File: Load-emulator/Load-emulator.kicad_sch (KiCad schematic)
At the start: 16 parts, among them J1 533980771, J2 SSW-126-04-G-D, J3 SSW-126-04-G-D, Q1 TIP41C, U1 LM324A

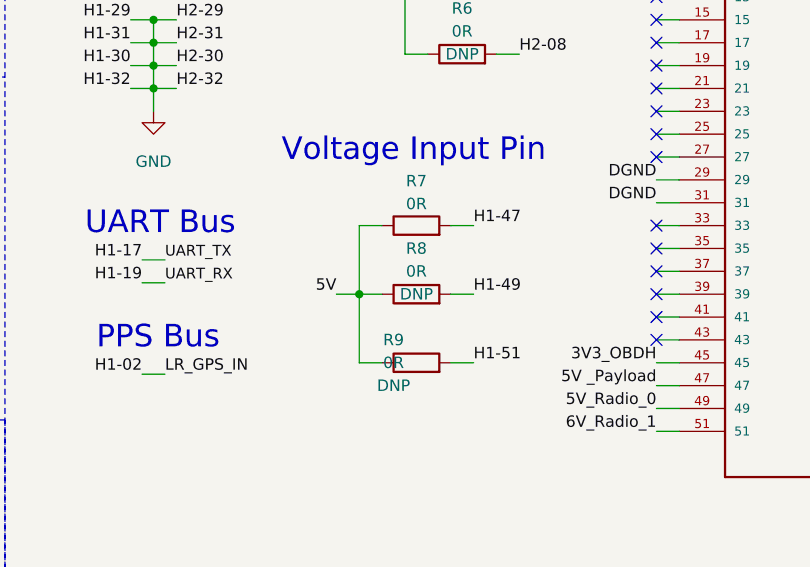
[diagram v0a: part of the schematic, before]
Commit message: Minor changes in schematic, add LM324N
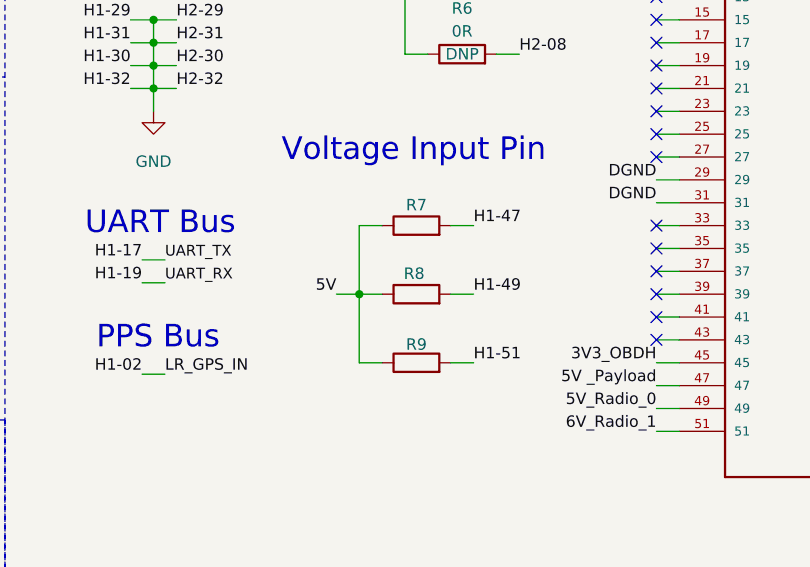
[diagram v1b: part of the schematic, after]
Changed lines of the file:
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@@
 		(dnp no)
 		(property "Reference" "R7"
-			(at 153.67 61.087 90)
+			(at 153.67 63.754 90)
 			(effects
 				(font
@@
 					(size 1.27 1.27)
 				)
+				(hide yes)
 			)
 		)
@@
 		(dnp no)
 		(property "Reference" "R9"
-			(at 151.13 78.74 90)
+			(at 153.67 79.248 90)
 			(effects
 				(font
@@
 		)
 		(property "Value" "0R"
-			(at 151.13 81.28 90)
-			(effects
-				(font
-					(size 1.27 1.27)
-				)
+			(at 155.194 83.82 90)
+			(effects
+				(font
+					(size 1.27 1.27)
+				)
+				(hide yes)
 			)
 		)
@@
 					(size 1.27 1.27)
 				)
+				(hide yes)
 			)
 		)
@@
 		(dnp no)
 		(property "Reference" "R8"
-			(at 153.67 68.58 90)
+			(at 153.416 71.374 90)
 			(effects
 				(font
@@
 					(size 1.27 1.27)
 				)
+				(hide yes)
 			)
 		)
@@
 					(size 1.27 1.27)
 				)
-			)
-		)
+				(hide yes)
+			)
+		)

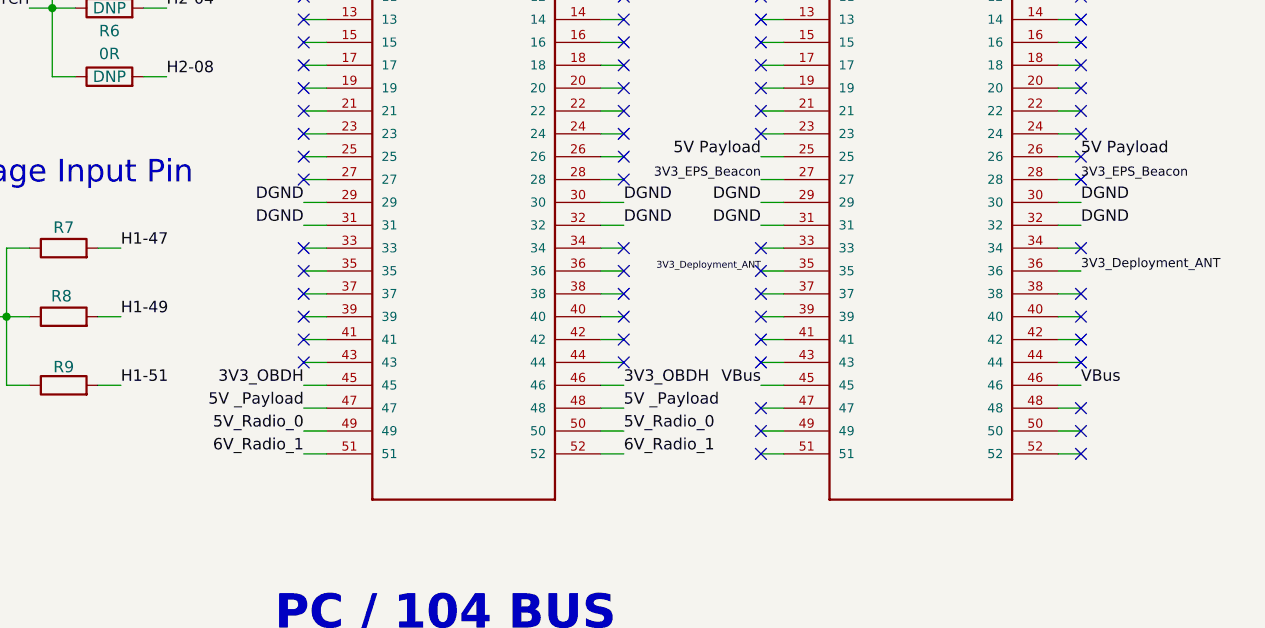
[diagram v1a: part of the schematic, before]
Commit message: Added new connector: PicoLock, as an alternative to the PC104. Connections between the two were made, so either one can be used.
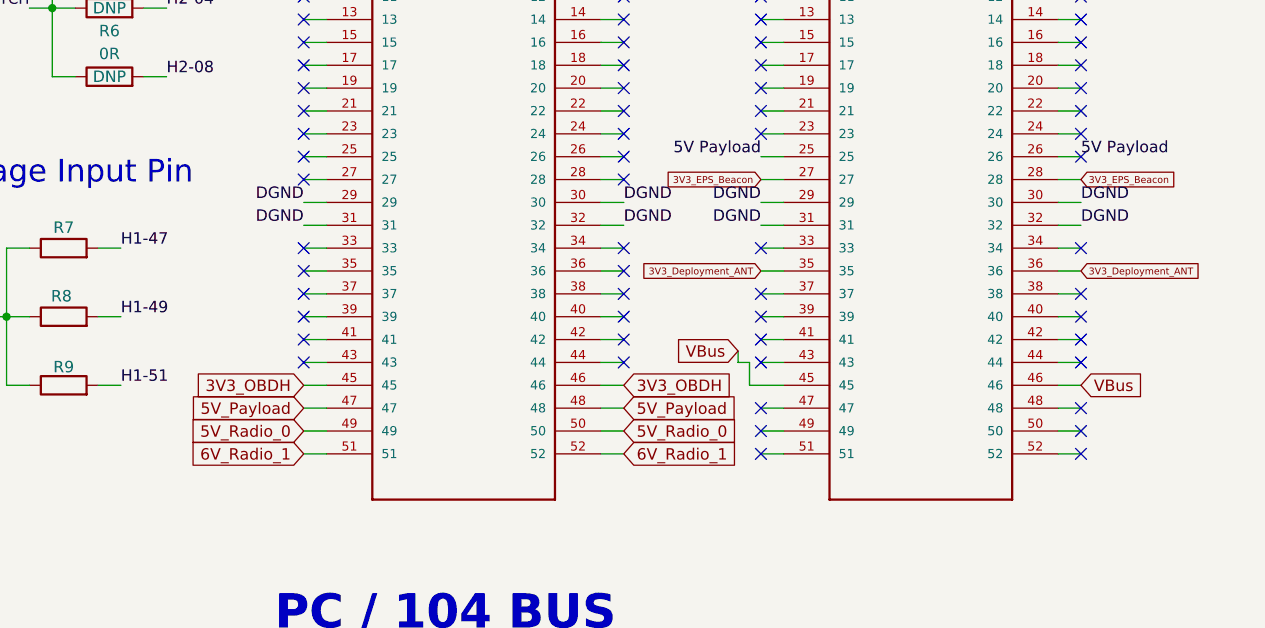
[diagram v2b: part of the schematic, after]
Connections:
- net 5V _Payload renamed 5V_Payload
- no-connect marks 83 -> 81

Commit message: Added footprints for the remaining resistors, capacitors and ampops, as well as some 3D models
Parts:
- Q1: footprint Package_TO_SOT_THT:TO-220-3_Vertical -> (none)
- R4, R5, R6, R7, R8, R9: footprint Resistor_SMD:R_0603_1608Metric_Pad0.98x0.95mm_HandSolder -> (none)
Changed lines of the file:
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@@
 			)
 		)
-		(property "Footprint" "Resistor_SMD:R_0603_1608Metric_Pad0.98x0.95mm_HandSolder"
+		(property "Footprint" ""
 			(at 158.75 41.148 90)
 			(effects
@@
 			)
 		)
-		(property "Footprint" "Resistor_SMD:R_0603_1608Metric_Pad0.98x0.95mm_HandSolder"
+		(property "Footprint" ""
 			(at 153.67 67.818 90)
 			(effects
@@
 			)
 		)
-		(property "Footprint" "Resistor_SMD:R_0603_1608Metric_Pad0.98x0.95mm_HandSolder"
+		(property "Footprint" ""
 			(at 153.67 83.058 90)
 			(effects
@@
 			)
 		)
-		(property "Footprint" "Resistor_SMD:R_0603_1608Metric_Pad0.98x0.95mm_HandSolder"
+		(property "Footprint" ""
 			(at 158.75 48.768 90)
 			(effects
@@
 			)
 		)
-		(property "Footprint" "Resistor_SMD:R_0603_1608Metric_Pad0.98x0.95mm_HandSolder"
+		(property "Footprint" ""
 			(at 158.75 33.528 90)
 			(effects
@@
 			)
 		)
-		(property "Footprint" "Resistor_SMD:R_0603_1608Metric_Pad0.98x0.95mm_HandSolder"
+		(property "Footprint" ""
 			(at 153.67 75.438 90)
 			(effects
@@
 			)
 		)
-		(property "Footprint" "Package_TO_SOT_THT:TO-220-3_Vertical"
+		(property "Footprint" ""
 			(at 81.28 112.395 0)
 			(effects

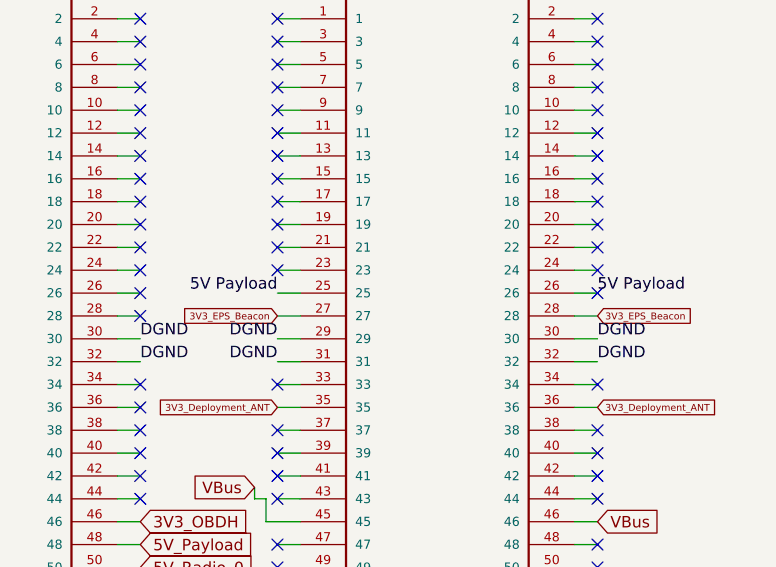
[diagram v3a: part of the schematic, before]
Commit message: File with 3D models were created, because the models were previously saved at a local PC, so only one specific machine could load them; Better organization; EPS terminal labels were added to each current sink channel; Channels were searched for possible errors
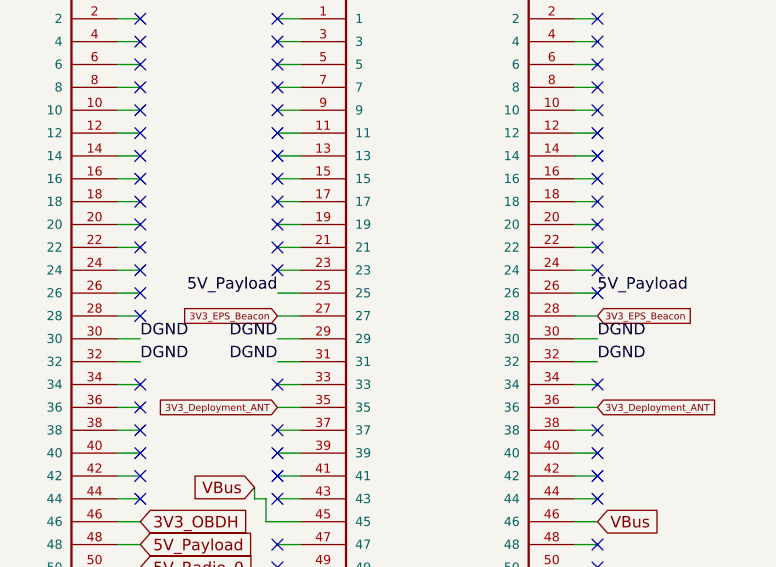
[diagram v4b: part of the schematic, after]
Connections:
- net 5V Payload is gone; now on net 5V_Payload: J3.25, J3.26
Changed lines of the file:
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@@
 		)
 	)
-	(label "5V Payload"
+	(label "5V_Payload"
 		(at 266.7 55.88 0)
 		(fields_autoplaced yes)
@@
 		)
 	)
-	(label "5V Payload"
+	(label "5V_Payload"
 		(at 231.14 55.88 180)
 		(fields_autoplaced yes)

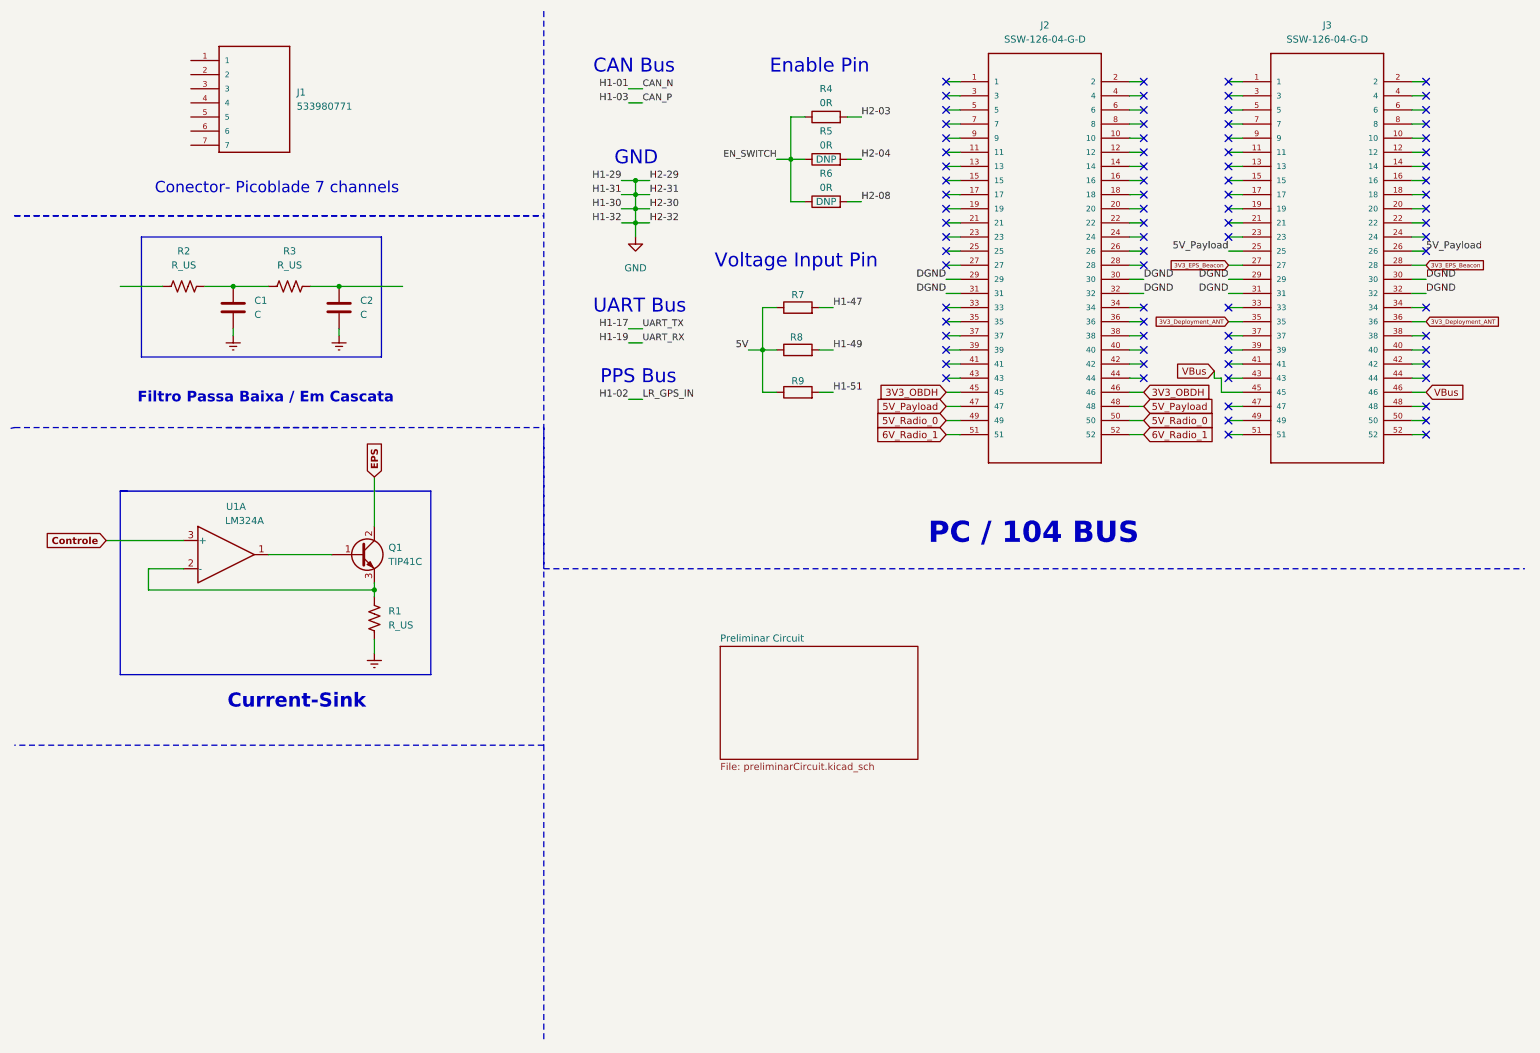
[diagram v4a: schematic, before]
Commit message: Rest of 3D models added, footprints added
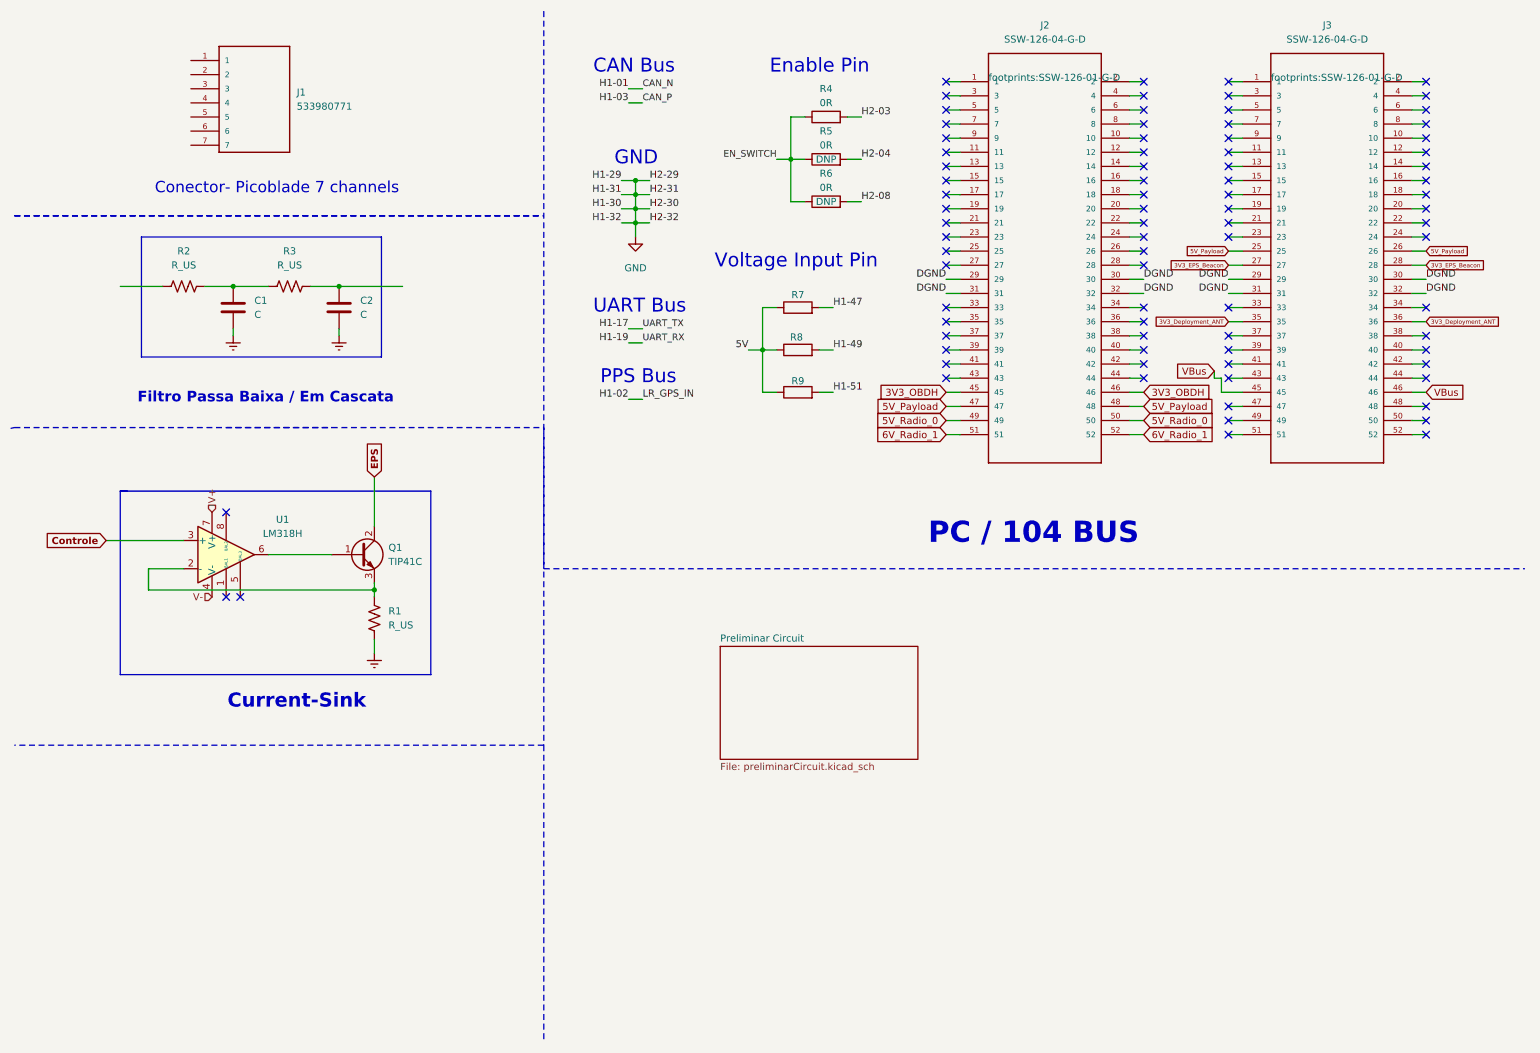
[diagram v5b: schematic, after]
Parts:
- removed U1: LM324A, symbol Amplifier_Operational:LM324A
- added U1: LM318H, symbol Amplifier_Operational:LM318H
- J3: footprint lib:TSW-126-07-X-D -> footprints:SSW-126-01-G-D
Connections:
- net Controle: now also U1.3 (+)
- net at Q1.3 (E), R1.1: now also U1.2 (-)
- net at Q1.1 (B): now also U1.6
- new net V+: U1.7 (V+)
- new net V-: U1.4 (V-)
- no-connect marks 81 -> 83
